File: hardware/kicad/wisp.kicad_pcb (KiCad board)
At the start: 2 copper layers, 140 x 100 mm, 73 parts, among them J1 USB-C, J2 Second I2C Bus, J3 mmWave UART (LD2410), J4 I2S Mic (INMP441), J5 Switched DC Output, J6 Reed/Hall Contact, J7 1-Wire Bus, J8 Analog Sensor Pad, J9 Expansion Header, Q1 MMBT3904, Q2 MMBT3904, Q3 2N7002, Q4 MMBT3904, SW1 RESET, SW2 BOOT, U1 CH340C, U2 AP63203WU-7, U3 ESP32-WROOM-32, U4 SCD41-D-R2, U5 BME680, U6 BH1750FVI-TR

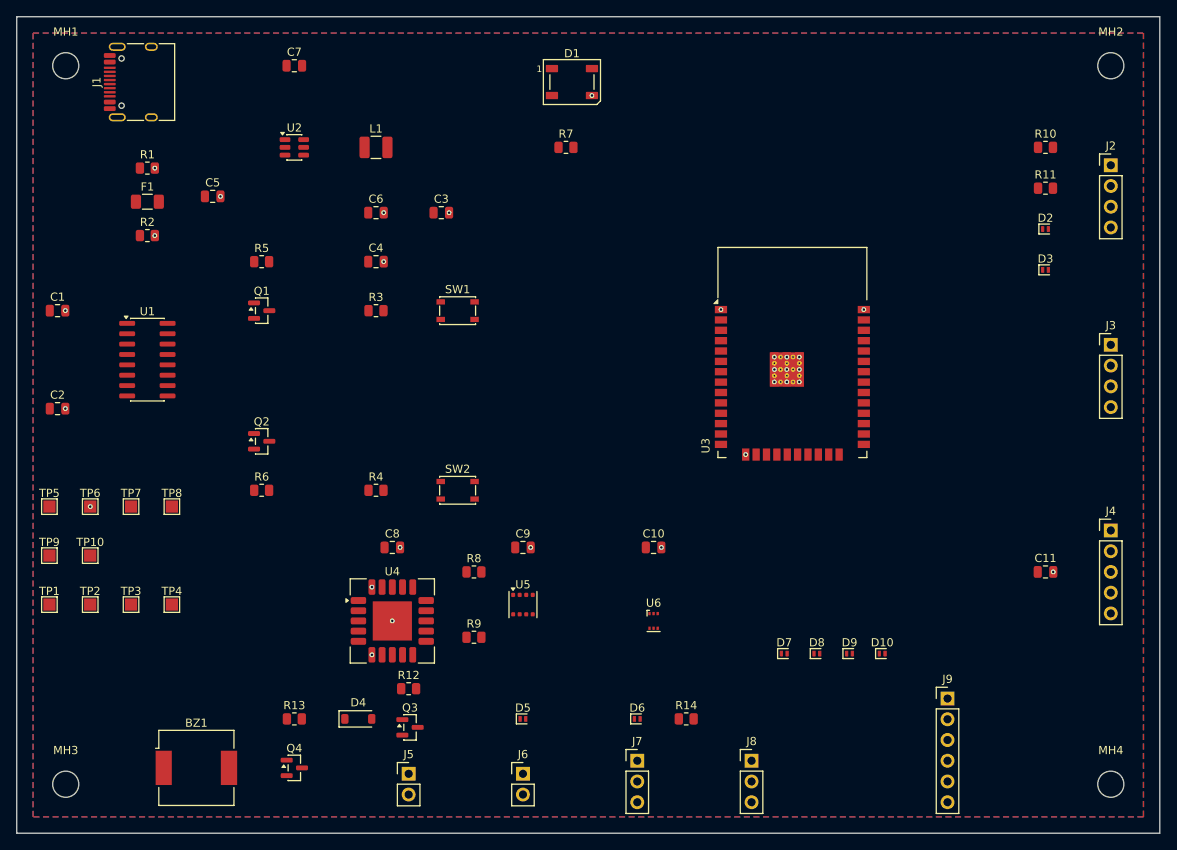
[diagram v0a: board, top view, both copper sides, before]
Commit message: Route all 44 signal nets, fix WROOM thermal-via drill size, generate fab Gerbers
Routed the board with Freerouting (headless, via a fetched jar) for the
bulk pass, then hand-closed a handful of nets/pour islands that
Freerouting's dense routing left disconnected, including rip-up/reroute
of a few local escape traces to free clearance. Also widened U3's
thermal-via array drill from 0.2mm to 0.3mm — undersized against the
board's own via_drill rule, previously masked because DRC only surfaces
that check once real routing exists.

DRC is 0 violations. One known gap remains: U5 pin 2 (+3V3) sits in a
fully enclosed pocket with no legal escape given its footprint's 0.8mm
pitch — documented in docs/hardware-expandability.md as a placement
fix for a future revision, not a routing one.

Gerbers and drill files exported to hardware/fab/gerbers/.

Co-Authored-By: Claude Sonnet 5 <noreply@anthropic.com>
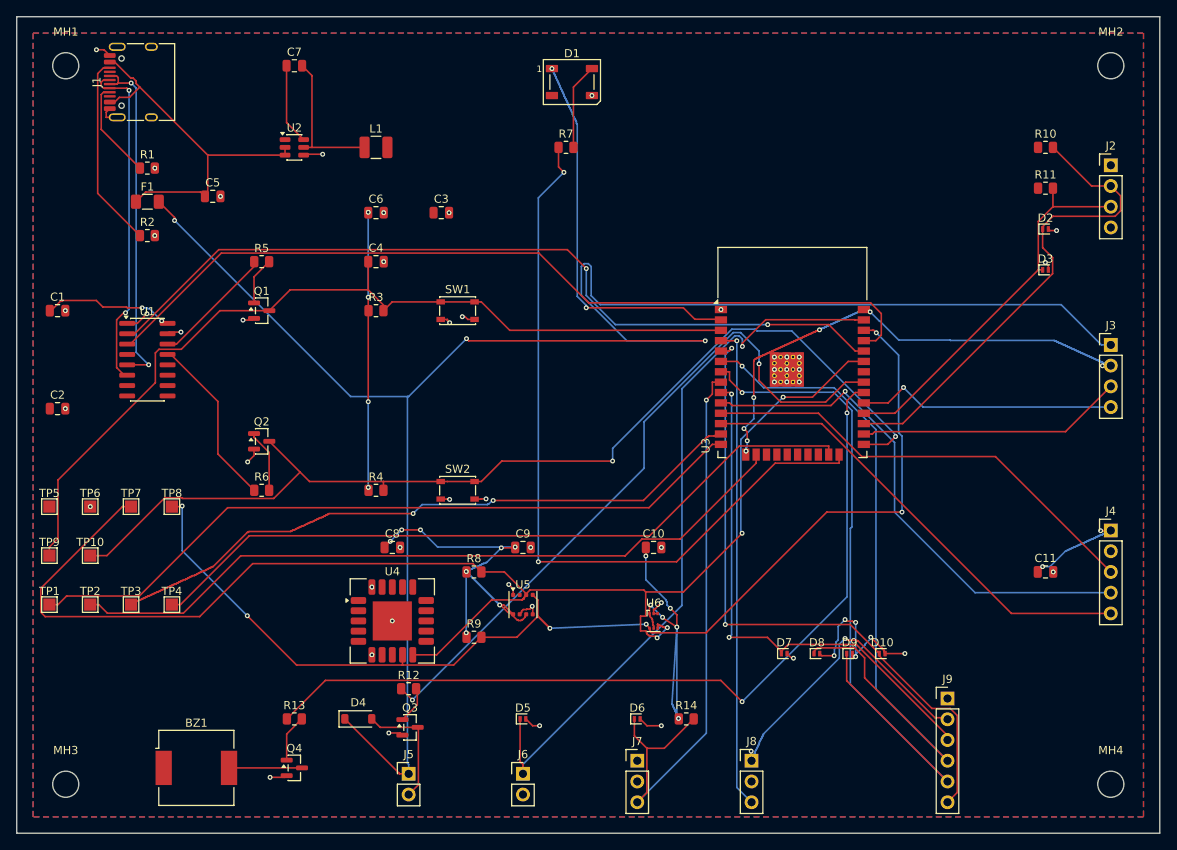
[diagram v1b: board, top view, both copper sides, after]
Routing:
- net +3V3: track 0.00 -> 243.9 mm, vias 0 -> 26
- net /+5V_EXT: track 0.00 -> 229.2 mm, vias 0 -> 3
- net /SDA: track 0.00 -> 171.9 mm, vias 0 -> 4
- net /SCL: track 0.00 -> 141.9 mm, vias 0 -> 6
- net /IO0: track 0.00 -> 128.3 mm, vias 0 -> 2
- net GND: track 0.00 -> 127.3 mm, vias 29 -> 60
- net /EN: track 0.00 -> 109.3 mm
- net /CH_RXD: track 0.00 -> 105.1 mm
- net /BUZZER_CTRL: track 0.00 -> 103.4 mm, vias 0 -> 2
- net /CH_TXD: track 0.00 -> 101.6 mm, vias 0 -> 2
- net /LED_CTRL: track 0.00 -> 95.2 mm, vias 0 -> 2
- net /JTAG_TCK: track 0.00 -> 90.7 mm
- net /EXP_IO34: track 0.00 -> 90.6 mm, vias 0 -> 1
- net /JTAG_TDI: track 0.00 -> 90.4 mm
- net /EXP_IO35: track 0.00 -> 89.9 mm, vias 0 -> 1
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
